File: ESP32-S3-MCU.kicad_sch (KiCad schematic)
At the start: 41 parts, among them SW1 RESET, SW2 RESET, U1 ESP32-S3, Y1 Crystal_GND24_Small

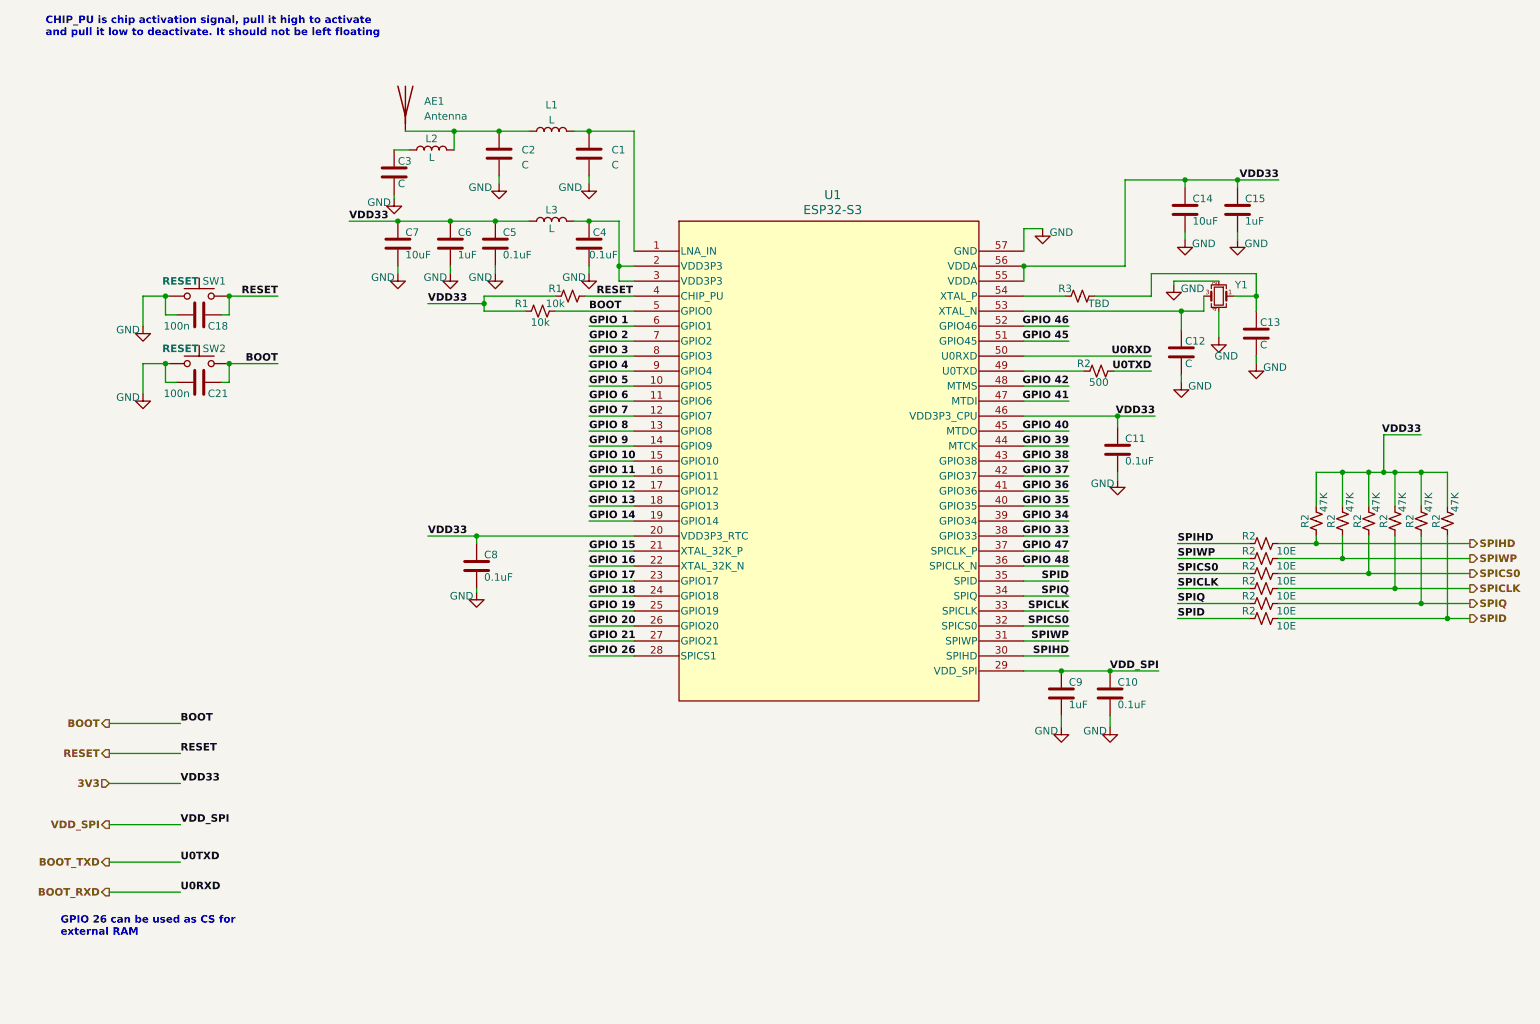
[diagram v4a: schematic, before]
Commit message: Added IP5306 for power path management
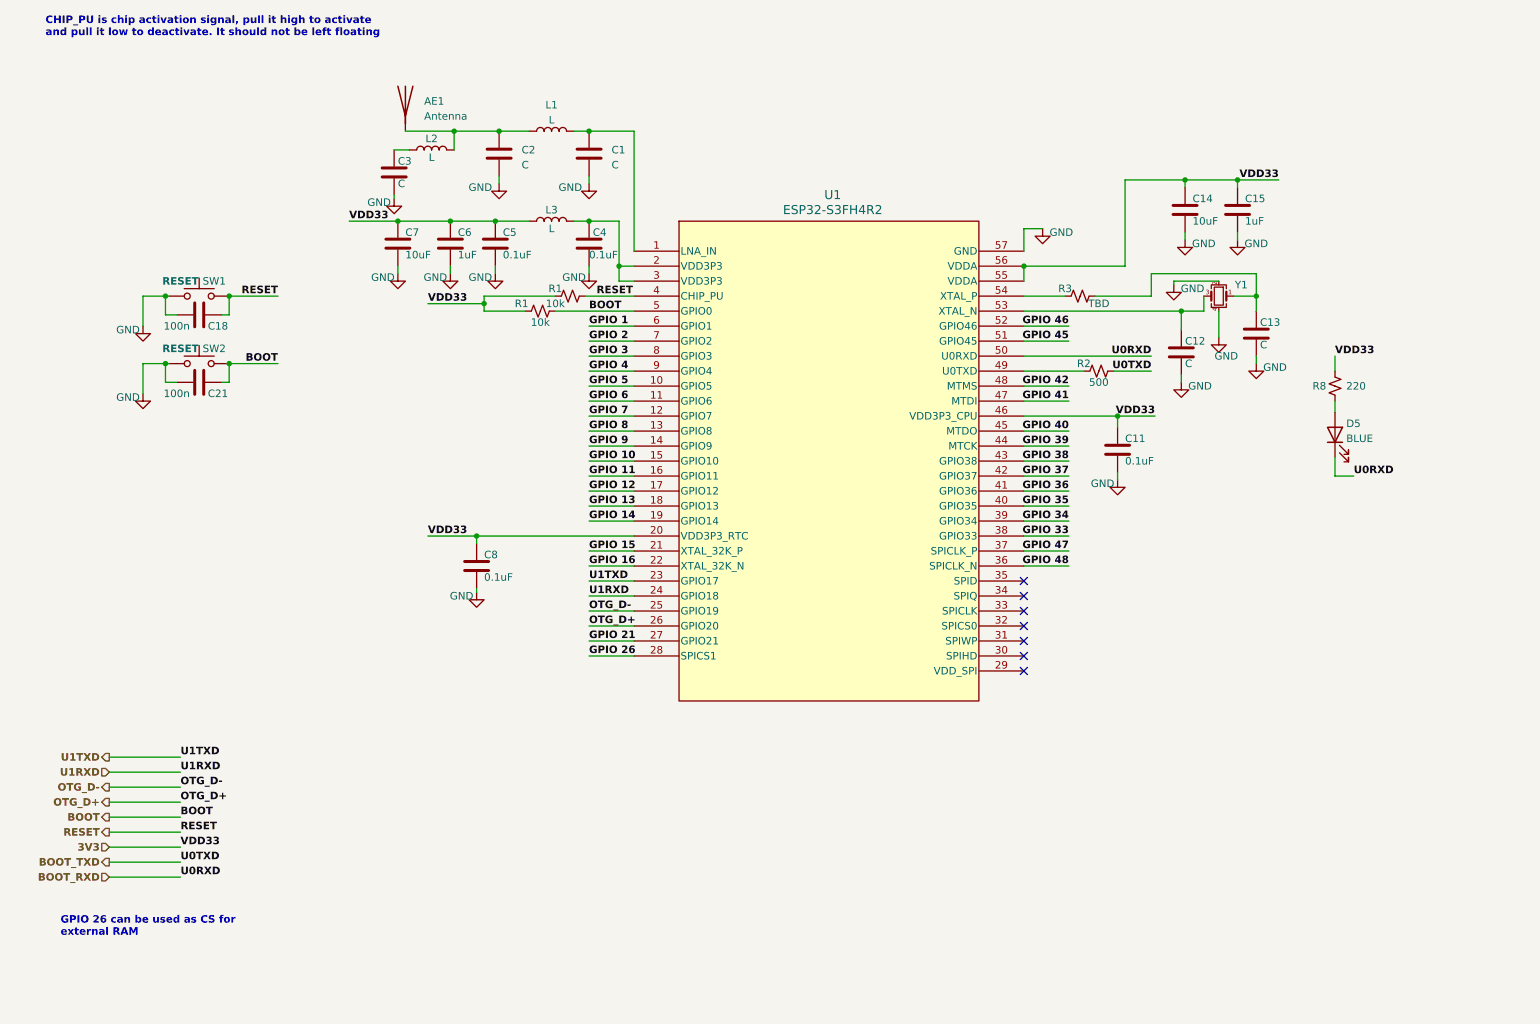
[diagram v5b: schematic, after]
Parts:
- removed C10: 0.1uF, symbol ESP32-S3_DB:C
- removed C9: 1uF, symbol ESP32-S3_DB:C
- removed R2 (x6): 10E, symbol ESP32-S3_DB:R_Small_US
- removed R2 (x6): 47K, symbol ESP32-S3_DB:R_Small_US
- added D5: BLUE, symbol ESP32-S3_DB:LED
- added R8: 220, symbol ESP32-S3_DB:R_Small_US
- U1: value ESP32-S3 -> ESP32-S3FH4R2
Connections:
- net 3V3: now also R8.1
- net BOOT_RXD: now also D5.1 (K)
- net GPIO 17 renamed U1TXD
- net GPIO 18 renamed U1RXD
- net GPIO 19 renamed OTG_D-
- net GPIO 20 renamed OTG_D+
- net SPICLK: no longer names the net of U1.33 (SPICLK)
- net SPICS0: no longer names the net of U1.32 (SPICS0)
- net SPID: no longer names the net of U1.35 (SPID)
- net SPIHD: no longer names the net of U1.30 (SPIHD)
- net SPIQ: no longer names the net of U1.34 (SPIQ)
- net SPIWP: no longer names the net of U1.31 (SPIWP)
- net VDD_SPI: no longer names the net of U1.29 (VDD_SPI)
- new net: D5.2 (A), R8.2
- no-connect marks 0 -> 7

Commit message: Assigned UART port 2 for RS-485
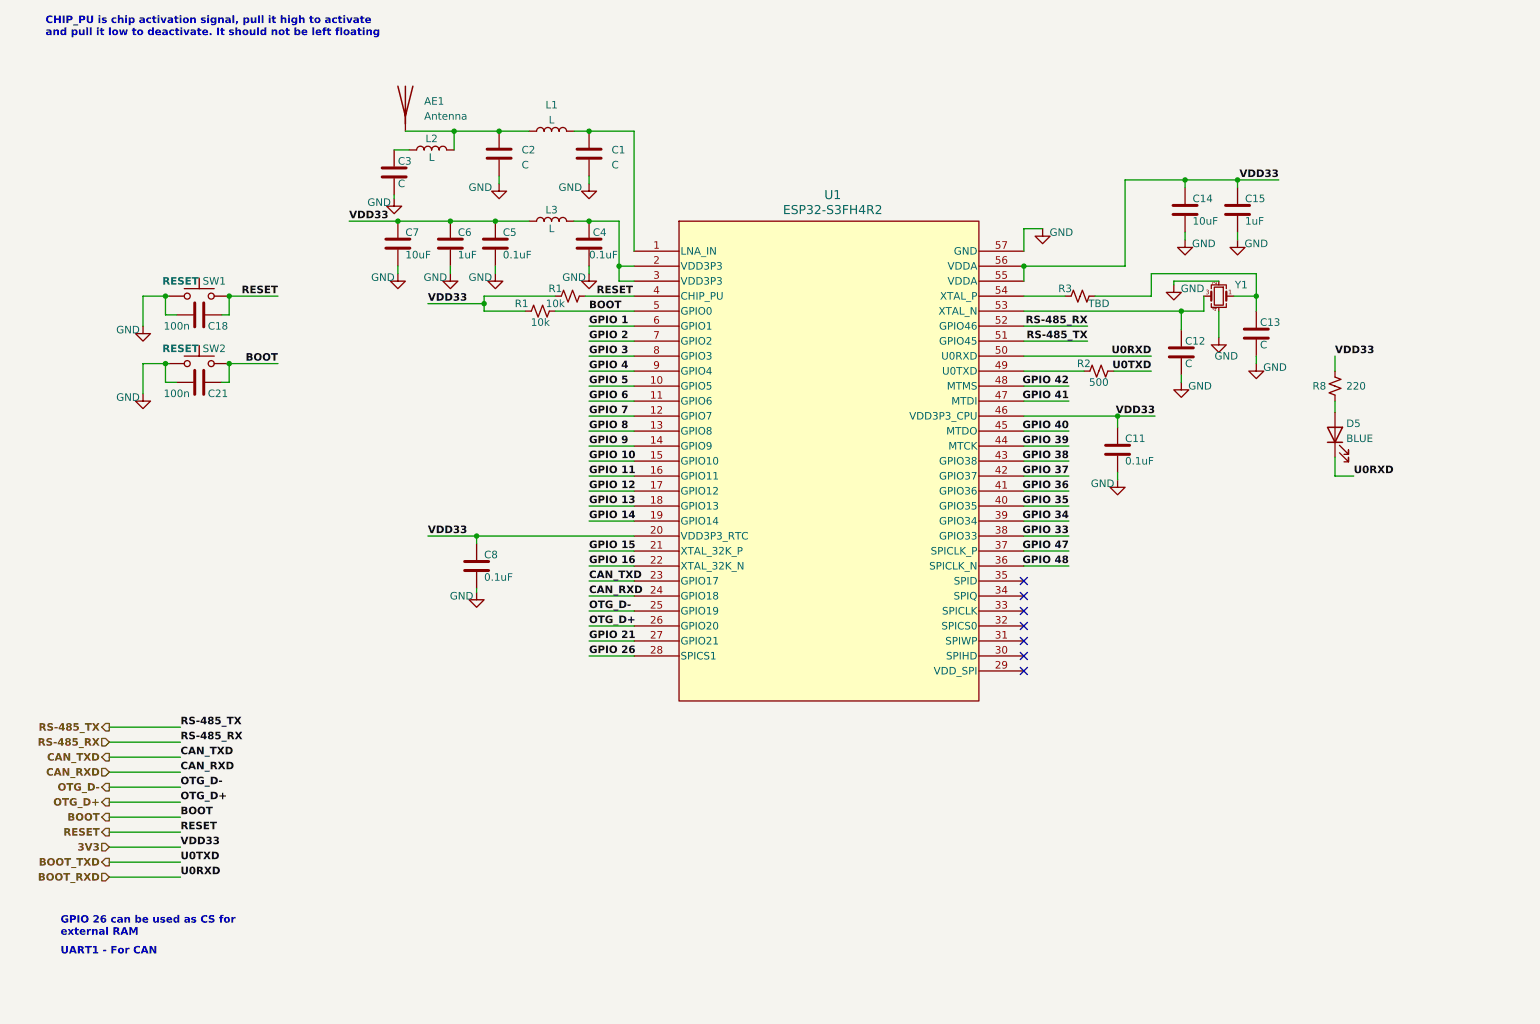
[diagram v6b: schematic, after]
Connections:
- net GPIO 45 renamed RS-485_TX
- net GPIO 46 renamed RS-485_RX
- net U1RXD renamed CAN_RXD
- net U1TXD renamed CAN_TXD
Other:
- note added: "UART1 - For CAN"
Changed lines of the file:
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@@
     (stroke (width 0) (type default))
   )
-  (wire (pts (xy 194.945 77.47) (xy 187.325 77.47))
+  (wire (pts (xy 198.12 77.47) (xy 187.325 77.47))
     (stroke (width 0) (type default))
   )
@@
     (stroke (width 0) (type default))
   )
-  (wire (pts (xy 194.945 74.93) (xy 187.325 74.93))
+  (wire (pts (xy 198.12 74.93) (xy 187.325 74.93))
     (stroke (width 0) (type default))
   )
@@
     (stroke (width 0) (type default))
   )
+  (wire (pts (xy 44.45 145.415) (xy 32.385 145.415))
+    (stroke (width 0.5) (type default))
+  )
   (wire (pts (xy 113.665 77.47) (xy 121.285 77.47))
     (stroke (width 0) (type default))
@@
     (stroke (width 0.5) (type default))
   )
+  (wire (pts (xy 44.45 142.875) (xy 32.385 142.875))
+    (stroke (width 0.5) (type default))
+  )
   (wire (pts (xy 223.52 50.165) (xy 223.52 51.435))
     (stroke (width 0) (type default))
@@
   (wire (pts (xy 187.325 69.85) (xy 194.31 69.85))
     (stroke (width 0) (type default))
+  )
+  (text "UART1 - For CAN" (at 24.13 181.61 0)
+    (effects (font (size 1.27 1.27) bold (color 0 0 255 1)) (justify left bottom))
   )
   (text "CHIP_PU is chip activation signal, pull it high to activate\nand pull it low to deactivate. It should not be left floating"
@@
     (effects (font (size 1.27 1.27) bold (color 0 0 255 1)) (justify left bottom))
   )
+  (label "CAN_TXD" (at 44.45 147.955 0) (fields_autoplaced)
+    (effects (font (size 1.27 1.27) bold (color 0 0 255 1)) (justify left bottom))
+  )
+  (label "RS-485_RX" (at 44.45 145.415 0) (fields_autoplaced)
+    (effects (font (size 1.27 1.27) bold (color 0 0 255 1)) (justify left bottom))
+  )
   (label "GPIO 14" (at 113.665 107.95 0) (fields_autoplaced)
     (effects (font (size 1.27 1.27) bold (color 255 0 255 1)) (justify left bottom))
@@
     (effects (font (size 1.27 1.27) bold (color 132 0 0 1)) (justify right bottom))
   )
-  (label "U1TXD" (at 113.665 118.11 0) (fields_autoplaced)
+  (label "CAN_TXD" (at 113.665 118.11 0) (fields_autoplaced)
     (effects (font (size 1.27 1.27) bold (color 0 0 255 1)) (justify left bottom))
   )
@@
     (effects (font (size 1.27 1.27) (thickness 0.254) bold (color 255 0 0 1)) (justify left bottom))
   )
+  (label "RS-485_TX" (at 44.45 142.875 0) (fields_autoplaced)
+    (effects (font (size 1.27 1.27) bold (color 0 0 255 1)) (justify left bottom))
+  )
   (label "RESET" (at 60.96 69.85 180) (fields_autoplaced)
     (effects (font (size 1.27 1.27) (thickness 0.254) bold (color 0 194 0 1)) (justify right bottom))
@@
     (effects (font (size 1.27 1.27) bold (color 255 0 255 1)) (justify left bottom))
   )
-  (label "U1TXD" (at 44.45 147.955 0) (fields_autoplaced)
-    (effects (font (size 1.27 1.27) bold (color 0 0 255 1)) (justify left bottom))
-  )
   (label "OTG_D+" (at 44.45 155.575 0) (fields_autoplaced)
     (effects (font (size 1.27 1.27) (thickness 0.254) bold (color 0 0 255 1)) (justify left bottom))
@@
     (effects (font (size 1.27 1.27) bold (color 255 0 255 1)) (justify left bottom))
   )
-  (label "GPIO 46" (at 194.945 74.93 180) (fields_autoplaced)
-    (effects (font (size 1.27 1.27) bold (color 255 0 255 1)) (justify right bottom))
-  )
   (label "GPIO 21" (at 113.665 128.27 0) (fields_autoplaced)
     (effects (font (size 1.27 1.27) bold (color 255 0 255 1)) (justify left bottom))
   )
-  (label "U1RXD" (at 113.665 120.65 0) (fields_autoplaced)
+  (label "CAN_RXD" (at 113.665 120.65 0) (fields_autoplaced)
     (effects (font (size 1.27 1.27) bold (color 0 0 255 1)) (justify left bottom))
   )
@@
     (effects (font (size 1.27 1.27) (thickness 0.254) bold (color 255 0 0 1)) (justify left bottom))
   )
+  (label "RS-485_TX" (at 198.12 77.47 180) (fields_autoplaced)
+    (effects (font (size 1.27 1.27) bold (color 0 0 255 1)) (justify right bottom))
+  )
   (label "U0TXD" (at 208.915 82.55 180) (fields_autoplaced)
     (effects (font (size 1.27 1.27) bold (color 0 0 255 1)) (justify right bottom))
@@
     (effects (font (size 1.27 1.27) bold (color 255 0 255 1)) (justify left bottom))
   )
+  (label "CAN_RXD" (at 44.45 150.495 0) (fields_autoplaced)
+    (effects (font (size 1.27 1.27) bold (color 0 0 255 1)) (justify left bottom))
+  )
   (label "GPIO 33" (at 194.945 110.49 180) (fields_autoplaced)
     (effects (font (size 1.27 1.27) bold (color 255 0 255 1)) (justify right bottom))
@@
     (effects (font (size 1.27 1.27) (thickness 0.254) bold (color 255 0 0 1)) (justify right bottom))
   )
-  (label "U1RXD" (at 44.45 150.495 0) (fields_autoplaced)
-    (effects (font (size 1.27 1.27) bold (color 0 0 255 1)) (justify left bottom))
-  )
   (label "VDD33" (at 73.025 57.15 0) (fields_autoplaced)
     (effects (font (size 1.27 1.27) (thickness 0.254) bold (color 255 0 0 1)) (justify left bottom))
   )
+  (label "RS-485_RX" (at 198.12 74.93 180) (fields_autoplaced)
+    (effects (font (size 1.27 1.27) bold (color 0 0 255 1)) (justify right bottom))
+  )
   (label "GPIO 34" (at 194.945 107.95 180) (fields_autoplaced)
-    (effects (font (size 1.27 1.27) bold (color 255 0 255 1)) (justify right bottom))
-  )
-  (label "GPIO 45" (at 194.945 77.47 180) (fields_autoplaced)
     (effects (font (size 1.27 1.27) bold (color 255 0 255 1)) (justify right bottom))
   )
@@
     (effects (font (size 1.27 1.27) bold (color 0 0 255 1)) (justify right))
   )
+  (hierarchical_label "RS-485_TX" (shape output) (at 32.385 142.875 180) (fields_autoplaced)
+    (effects (font (size 1.27 1.27) (thickness 0.254) bold (color 0 0 255 1)) (justify right))
+  )
   (hierarchical_label "BOOT" (shape output) (at 32.385 158.115 180) (fields_autoplaced)
     (effects (font (size 1.27 1.27) bold (color 132 0 0 1)) (justify right))
@@
     (effects (font (size 1.27 1.27) bold (color 0 0 255 1)) (justify right))
   )
-  (hierarchical_label "U1RXD" (shape input) (at 32.385 150.495 180) (fields_autoplaced)
+  (hierarchical_label "CAN_RXD" (shape input) (at 32.385 150.495 180) (fields_autoplaced)
     (effects (font (size 1.27 1.27) bold (color 0 0 255 1)) (justify right))
   )
@@
     (effects (font (size 1.27 1.27) bold (color 0 0 255 1)) (justify right))
   )
-  (hierarchical_label "U1TXD" (shape output) (at 32.385 147.955 180) (fields_autoplaced)
+  (hierarchical_label "RS-485_RX" (shape input) (at 32.385 145.415 180) (fields_autoplaced)
+    (effects (font (size 1.27 1.27) (thickness 0.254) bold (color 0 0 255 1)) (justify right))
+  )
+  (hierarchical_label "CAN_TXD" (shape output) (at 32.385 147.955 180) (fields_autoplaced)
     (effects (font (size 1.27 1.27) bold (color 0 0 255 1)) (justify right))
   )
   (hierarchical_label "3V3" (shape input) (at 32.385 163.195 180) (fields_autoplaced)
-    (effects (font (size 1.27 1.27) (thickness 0.254) bold) (justify right))
+    (effects (font (size 1.27 1.27) (thickness 0.254) bold (color 255 0 0 1)) (justify right))
   )
   (symbol (lib_id "ESP32-S3_DB:GND") (at 98.425 50.8 0) (unit 1)

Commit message: Added SD card interface
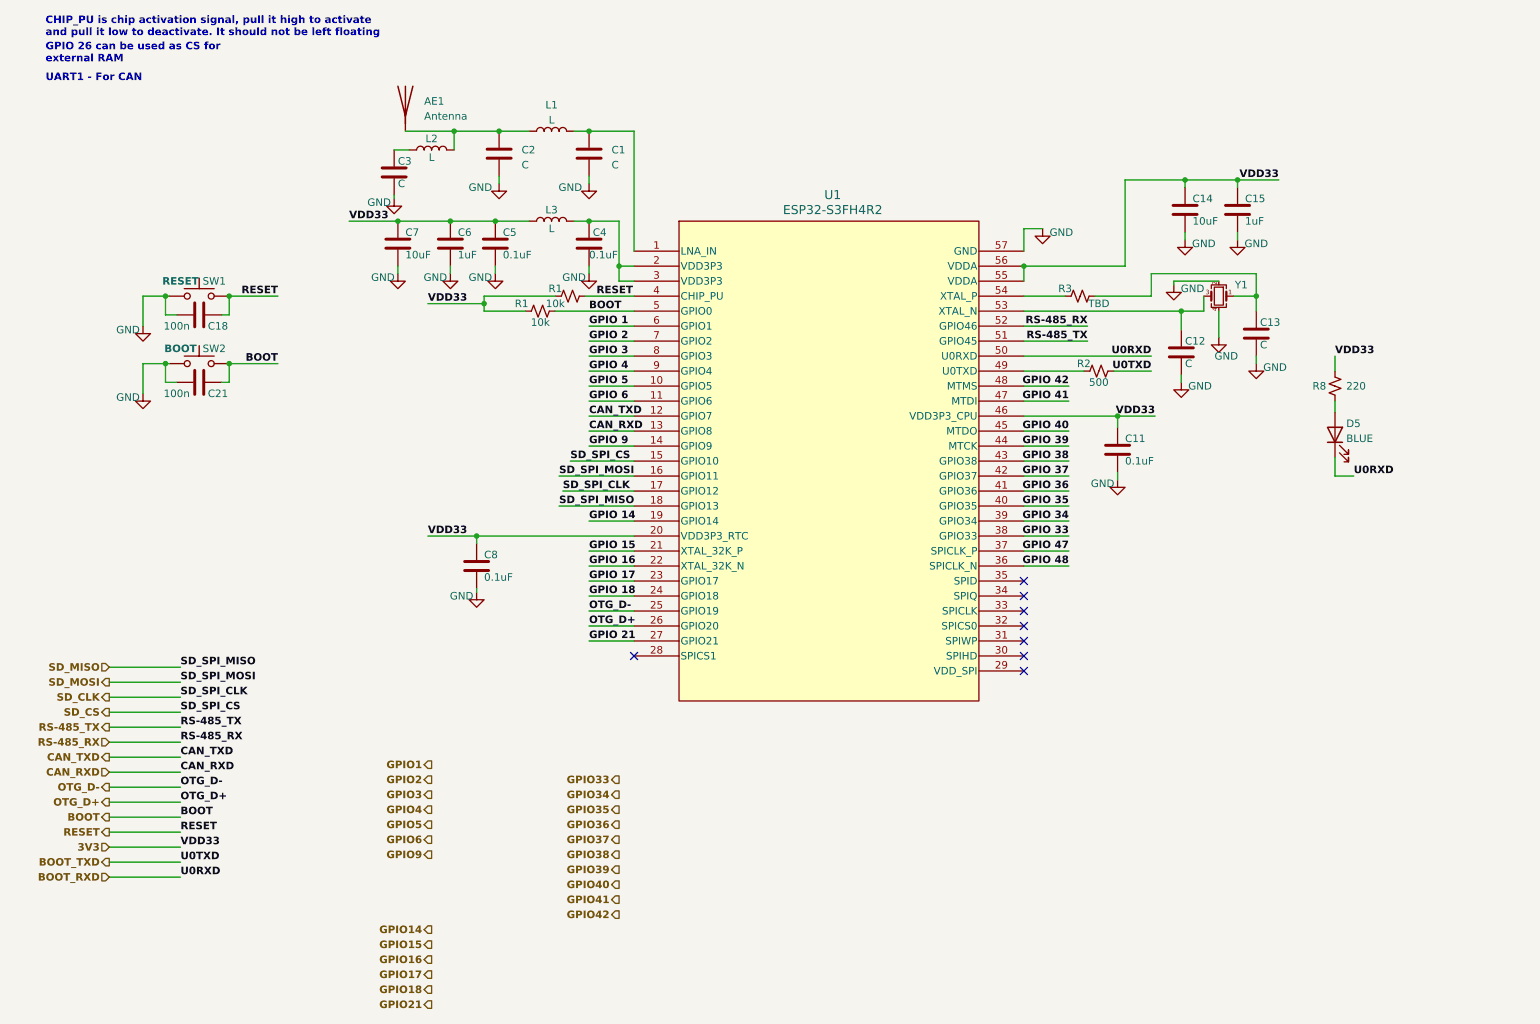
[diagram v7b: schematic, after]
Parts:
- SW2: value RESET -> BOOT
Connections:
- net GPIO 7 is gone; now on net CAN_TXD: U1.12 (GPIO7)
- net GPIO 8 is gone; now on net CAN_RXD: U1.13 (GPIO8)
- net CAN_RXD: no longer U1.24 (GPIO18)
- net CAN_TXD: no longer U1.23 (GPIO17)
- net GPIO 10 renamed SD_CS
- net GPIO 11 renamed SD_MOSI
- net GPIO 12 renamed SD_CLK
- net GPIO 13 renamed SD_MISO
- net GPIO 26: no longer names the net of U1.28 (SPICS1)
- new net GPIO 17: U1.23 (GPIO17)
- new net GPIO 18: U1.24 (GPIO18)
- no-connect marks 7 -> 8
